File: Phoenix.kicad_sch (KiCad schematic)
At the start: 2 parts

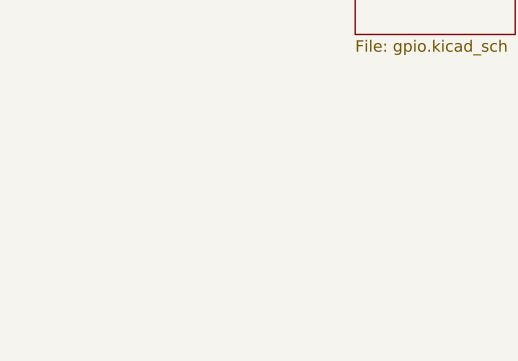
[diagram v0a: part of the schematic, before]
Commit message: Centered RP2040, added mounting hardware, Rearranged radio
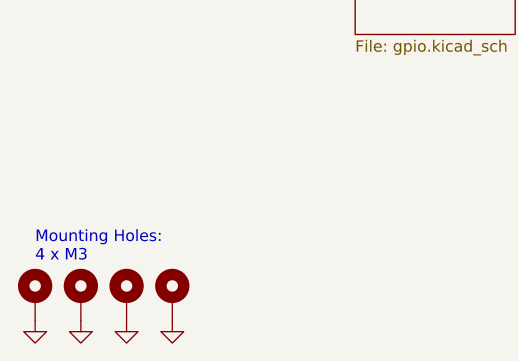
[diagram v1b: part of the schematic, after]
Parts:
- added H1, H2, H3, H4: MountingHole_Pad, MountingHole:MountingHole_3.2mm_M3_ISO7380_Pad_TopBottom, symbol Mechanical:MountingHole_Pad
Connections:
- new net GND: H1.1, H2.1, H3.1, H4.1
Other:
- note added: "Mounting Holes: 4 x M3"

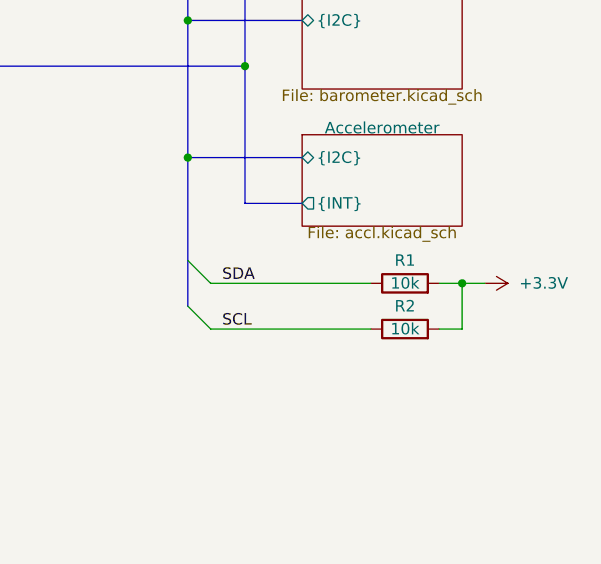
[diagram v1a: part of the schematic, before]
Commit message: Geographical reannotated
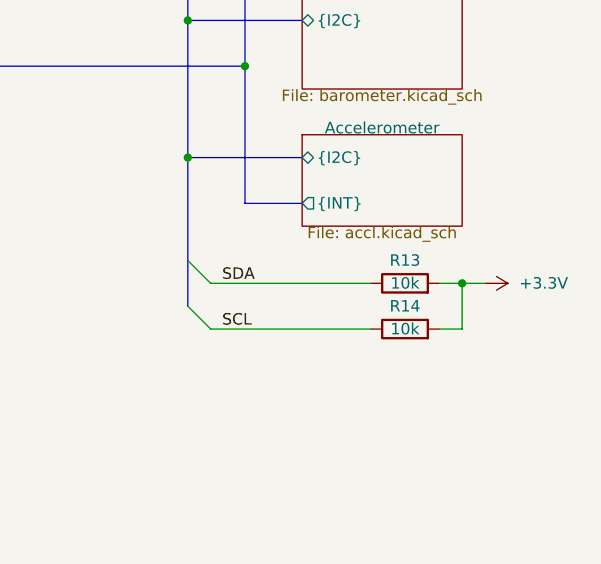
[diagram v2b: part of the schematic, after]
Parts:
- renumbered H2 to H1, H3 to H2, H1 to H3, R1 to R13, R2 to R14

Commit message: Final refinements before issue to JLC
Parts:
- added TP1, TP2, TP3, TP4: TestPoint_Flag, TestPoint:TestPoint_Pad_D1.5mm, symbol Connector:TestPoint_Flag
- renumbered H3 to H1, H1 to H2, H2 to H3, R13 to R1, R14 to R2
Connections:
- net +3V3: now also TP3.1
- net GND: now also TP4.1
- net SCL: now also TP2.1
- net SDA: now also TP1.1

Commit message: Reorganised repo
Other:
- sheet Accelerometer: file accl.kicad_sch -> ./Peripherals/accl.kicad_sch
- sheet Barometer: file barometer.kicad_sch -> ./Peripherals/barometer.kicad_sch
- sheet Flash Storage: file flash.kicad_sch -> ./Peripherals/flash.kicad_sch
- sheet GPIO & Pyro: file gpio.kicad_sch -> ./Peripherals/gpio.kicad_sch
- sheet GPS: file gps.kicad_sch -> ./Peripherals/gps.kicad_sch
- sheet Gyroscope: file gyro.kicad_sch -> ./Peripherals/gyro.kicad_sch
- sheet Radio: file radio.kicad_sch -> ./Peripherals/radio.kicad_sch
